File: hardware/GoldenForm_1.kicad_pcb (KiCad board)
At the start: 4 copper layers, 60 x 45.3 mm, 60 parts, among them IC1 UVLO, J1 1140084168, J2 Conn_01x02_Pin, J3 USB4105-GF-A, J4 Conn_01x04_Pin, J5 Conn_01x02_Pin, M1 MountingHole x 4, U1 ESP32-S3-WROOM-1, U2 BNO055, U3 Buck_Boost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

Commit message: WIP
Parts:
- J3: moved to B.Cu

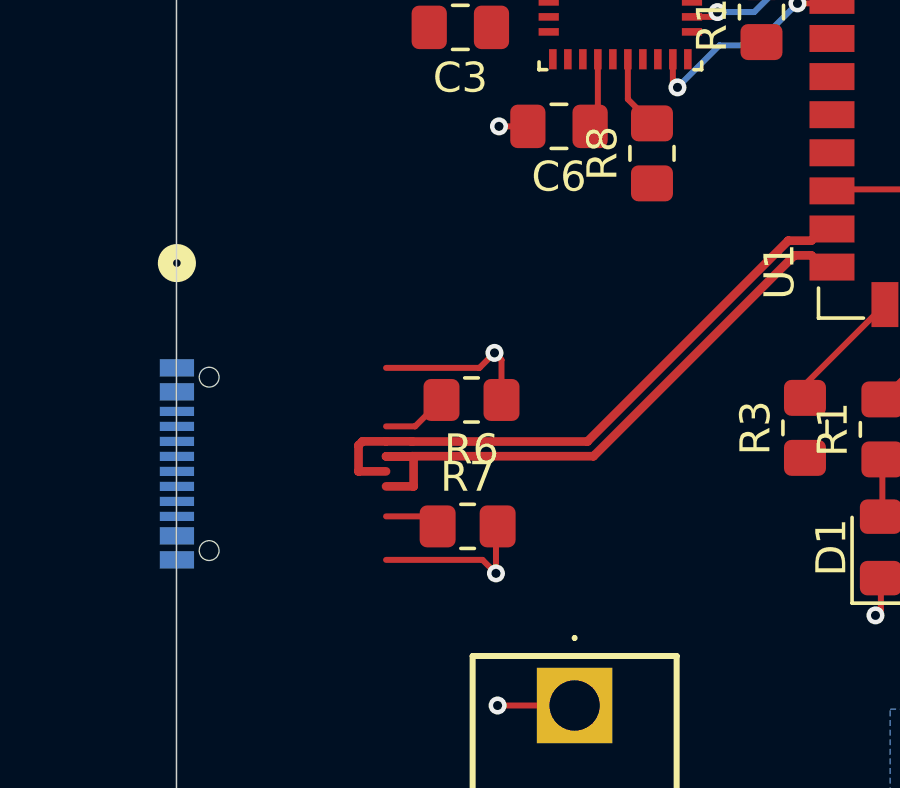
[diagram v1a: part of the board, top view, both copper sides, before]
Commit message: WIP ESD protection for USB receptacle
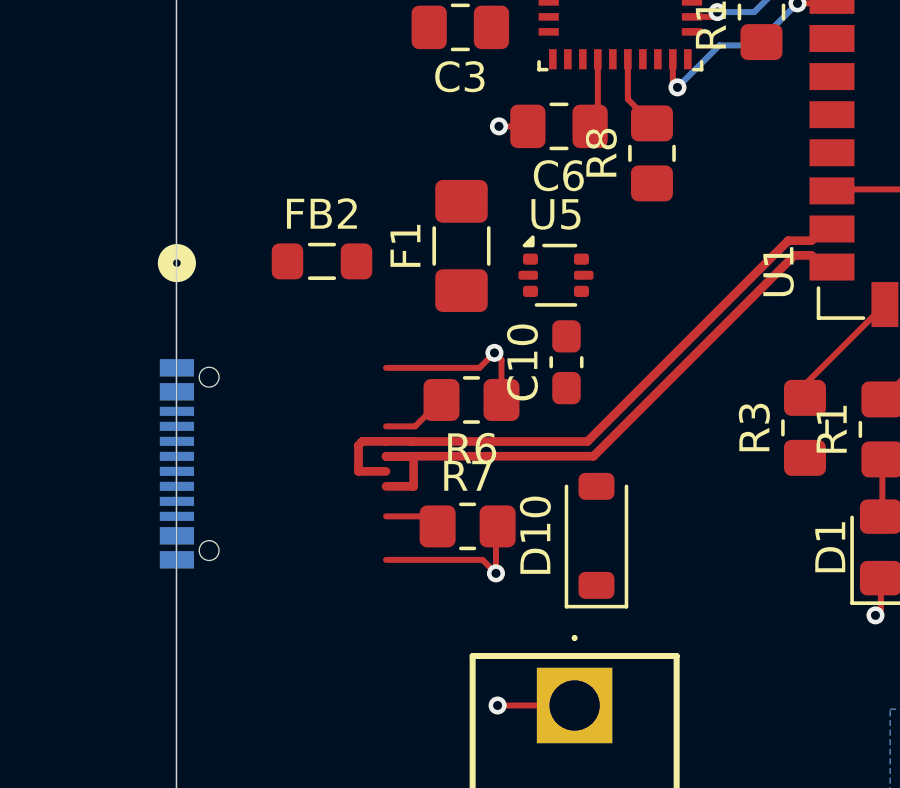
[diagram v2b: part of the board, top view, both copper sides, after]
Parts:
- added C10: 100nF, Capacitor_SMD:C_0603_1608Metric_Pad1.08x0.95mm_HandSolder, F.Cu at (80.5, 71.4)
- added D10: 1N5817, Diode_SMD:D_SOD-123, F.Cu at (81.5, 77.2)
- added F1: Polyfuse, Fuse:Fuse_1206_3216Metric_Pad1.42x1.75mm_HandSolder, F.Cu at (77.0, 67.5)
- added FB2: BLM21PG220, Inductor_SMD:L_0805_2012Metric_Pad1.05x1.20mm_HandSolder, F.Cu at (72.3, 68.0)
- added U5: USBLC6-2P6, Package_TO_SOT_SMD:SOT-666, F.Cu at (80.2, 68.5)
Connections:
- net V_BUS renamed Net-(F1-Pad1)
- J3 pad A6: D+ -> DP1
- J3 pad A7: D- -> DN1
- J3 pad B6: D+ -> DP1
- J3 pad B7: D- -> DN1
- U1 pad 13: D- -> /USB_D+
- U1 pad 14: D+ -> /USB_D-
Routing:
- net D+: track 20.6 -> 0.00 mm
- net /USB_D-: track 0.00 -> 20.6 mm
- net D-: track 20.6 -> 0.00 mm
- net /USB_D+: track 0.00 -> 20.6 mm
